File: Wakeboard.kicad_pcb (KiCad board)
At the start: 2 copper layers, 30.6 x 58.6 mm, 34 parts, among them CN1 JST S2B-PH-SM4-TB(LF)(SN), J2 HCTL HC-TYPE-C-16P-01A, Q1 DMP2045UQ-7, SW1 TS-1088-AR02016, SW2 TS-1088-AR02016, U1 RT9080-33GJ5, U2 ESP32-S3-MINI-1, U3 LIS3DHTR_C15134, U4 MCP73831T-2ACI/OT

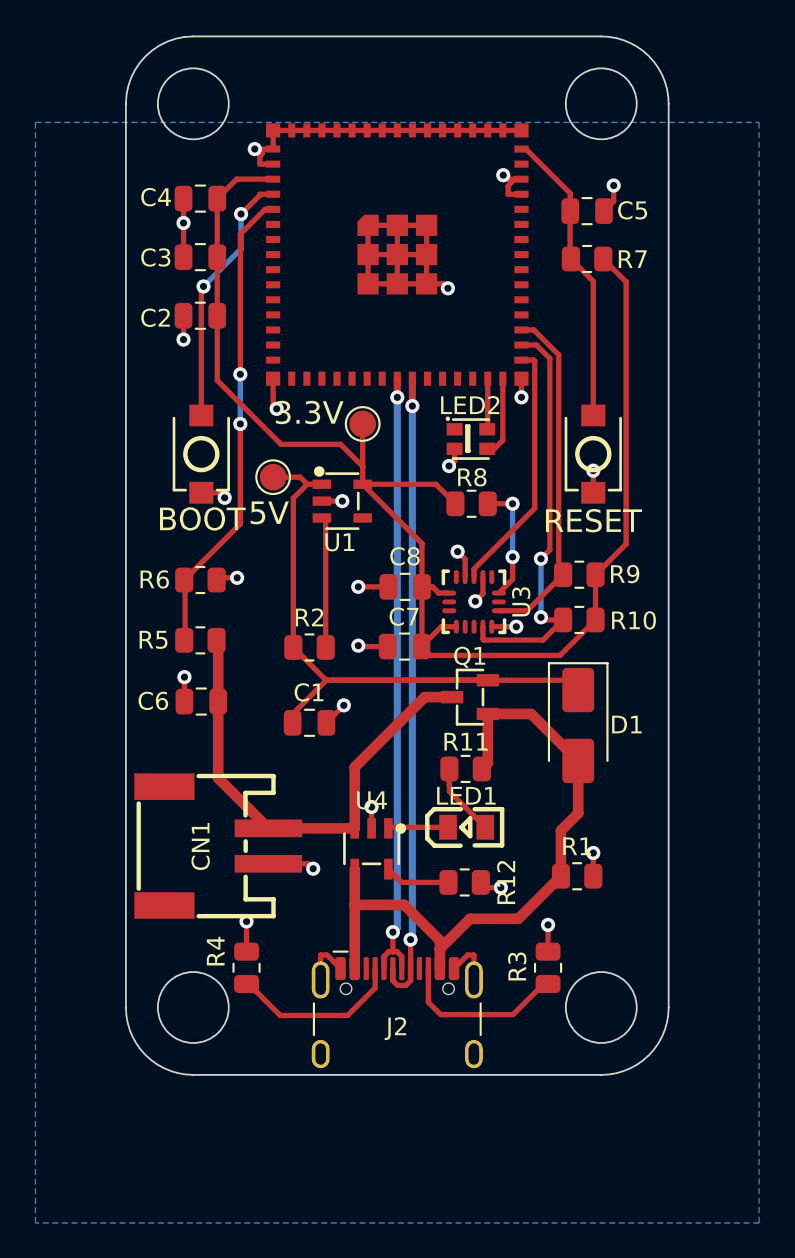
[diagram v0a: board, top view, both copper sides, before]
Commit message: Remove PCB below antenna. Swap SDA and SCL GPIO. Update interrupt to GPIO 21, battery level to GPIO 10.
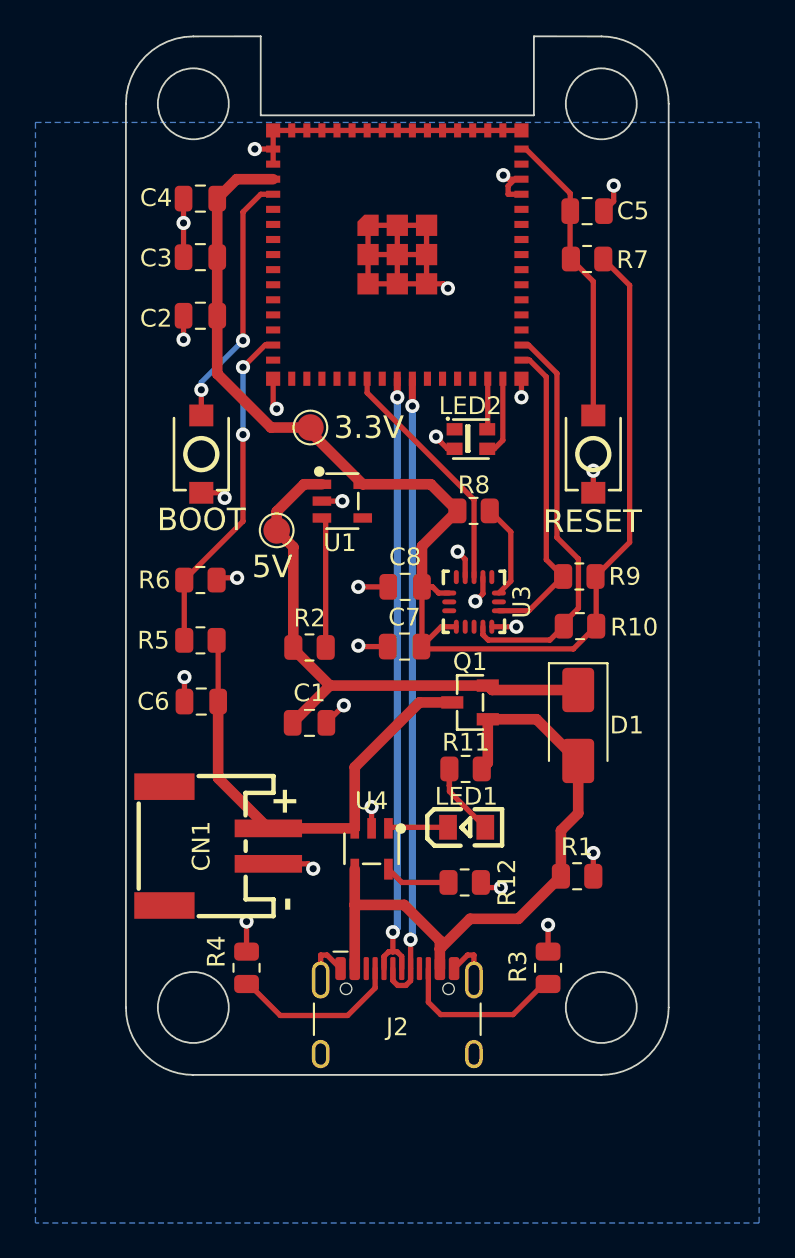
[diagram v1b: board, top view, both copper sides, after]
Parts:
- TP1: value TestPoint -> 5V
- TP2: value TestPoint -> 3.3V
- moved TP1 3.01 mm to (120.7, 72.3)
- moved TP2 2.96 mm to (122.6, 66.5)
- moved R8 0.42 mm to (131.8, 71.2)
- moved R10 0.35 mm to (137.8, 77.7)
- moved Q1 0.30 mm to (131.6, 82.0)
- moved R9 0.10 mm to (137.8, 74.9)
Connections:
- R5 pad 1: GPIO1 -> BAT_SENS
- R6 pad 2: GPIO1 -> BAT_SENS
- U2 pad 14: unconnected-(U2-IO10-Pad14) -> BAT_SENS
- U2 pad 21: unconnected-(U2-IO17-Pad21) -> INT1
- U2 pad 31: INT1 -> SDA
- U2 pad 33: SDA -> unconnected-(U2-IO37-Pad33)
- U2 pad 5: GPIO1 -> unconnected-(U2-IO1-Pad5)
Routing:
- net GPIO1: track 26.8 -> 0.00 mm, vias 2 -> 0
- net BAT_SENS: track 0.00 -> 19.0 mm, vias 0 -> 2
- net Net-(D1-K): track 42.6 -> 31.3 mm
- net 3.3V: track 80.3 -> 75.6 mm
- net SDA: track 19.6 -> 17.9 mm
- net Net-(U3-CS): track 6.75 -> 5.40 mm, vias 2 -> 0
- net INT1: track 14.4 -> 13.7 mm
- net SCL: track 23.7 -> 23.2 mm, vias 2 -> 0
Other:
- outline, holes or cut-outs redrawn
- board text added: "+"
- board text added: "-"
